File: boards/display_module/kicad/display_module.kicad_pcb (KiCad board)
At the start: 2 copper layers, 58.4 x 148.6 mm, 31 parts, among them IC1 ATMEGA328-P, P1 CONN_01X02, Q1 NDP6020P, Q2 NDP6020P, Q3 NDP6020P, Q4 NDP6020P, Q5 NDP6020P, Q6 NDP6020P, Q7 NDP6020P, Q8 NDP6020P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

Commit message: display module design
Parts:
- moved C1 60.2 mm to (185.4, 44.5)
- moved R8 55.9 mm to (188.0, 52.1)
- moved C4 14.4 mm to (160.0, 52.1)
- moved U2 2.84 mm to (132.1, 64.8)
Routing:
- net Net-(DISP1-Pad9): track 70.5 -> 0.00 mm
- net Net-(DISP1-Pad3): track 70.5 -> 0.00 mm
- net Net-(DISP1-Pad12): track 68.1 -> 0.00 mm
- net Net-(DISP1-Pad6): track 68.1 -> 0.00 mm
- net Net-(DISP1-Pad19): track 59.5 -> 0.00 mm
- net Net-(DISP1-Pad13): track 59.5 -> 0.00 mm
- net Net-(DISP1-Pad16): track 59.5 -> 0.00 mm
- net Net-(DISP1-Pad22): track 59.5 -> 0.00 mm
- net Net-(DISP2-Pad14): track 55.4 -> 0.00 mm
- net Net-(DISP2-Pad1): track 55.4 -> 0.00 mm
- net Net-(DISP2-Pad2): track 54.7 -> 0.00 mm
- net Net-(DISP2-Pad4): track 52.9 -> 0.00 mm
- net Net-(DISP2-Pad5): track 52.2 -> 0.00 mm
- net Net-(DISP2-Pad8): track 47.0 -> 0.00 mm
- net Net-(DISP2-Pad7): track 45.9 -> 0.00 mm
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- removed copper zone on F.Cu, net GND

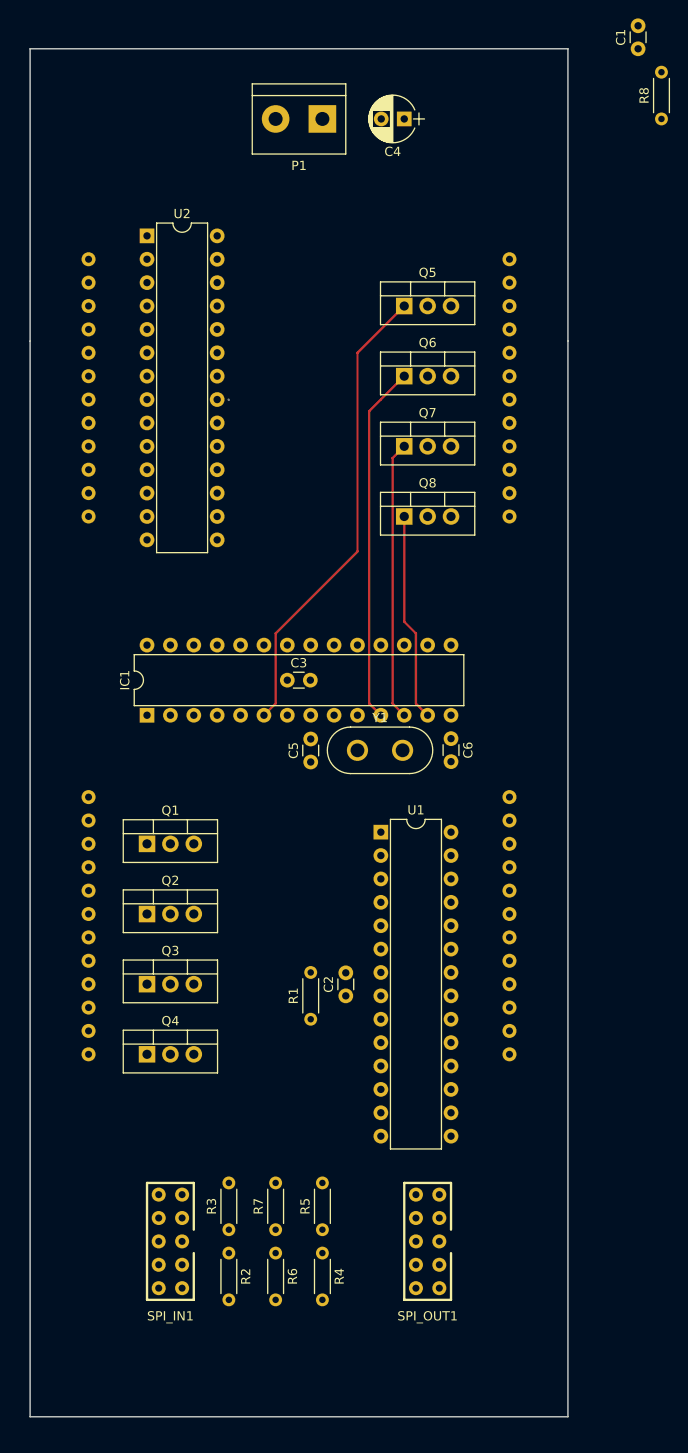
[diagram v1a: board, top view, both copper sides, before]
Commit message: finished display module layout, sent to printing
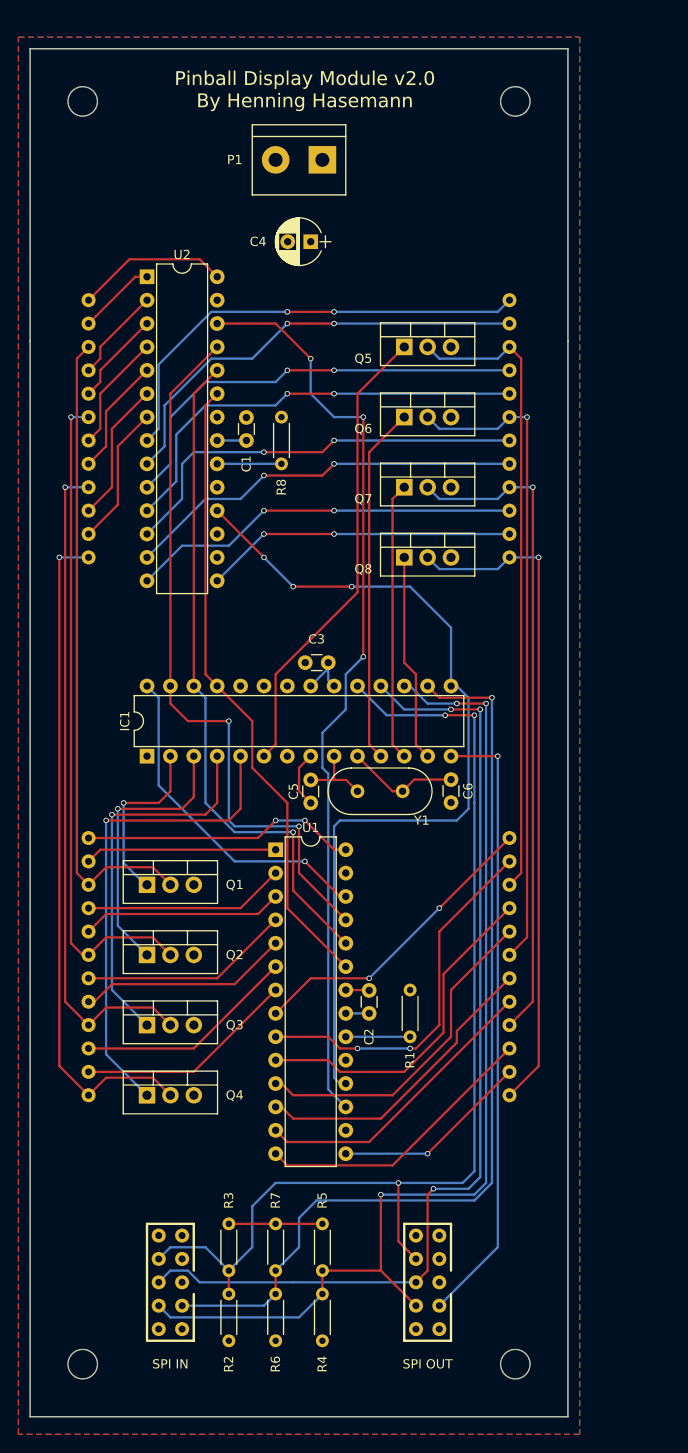
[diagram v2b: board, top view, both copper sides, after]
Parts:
- added ?: , Mounting_Holes:MountingHole_3.2mm_M3_DIN965, F.Cu at (125.1, 50.2)
- added ?: , Mounting_Holes:MountingHole_3.2mm_M3_DIN965, F.Cu at (172.1, 50.2)
- added ?: , Mounting_Holes:MountingHole_3.2mm_M3_DIN965, F.Cu at (172.1, 187.3)
- added ?: , Mounting_Holes:MountingHole_3.2mm_M3_DIN965, F.Cu at (125.1, 187.3)
- SPI IN: renamed from SPI_IN1
- SPI OUT: renamed from SPI_OUT1
- Y1: footprint Crystals:Crystal_HC50_Vertical -> Crystals:Crystal_HC18-U_Vertical
- moved C1 60.2 mm to (142.9, 87.0)
- moved R8 55.7 mm to (146.7, 89.5)
- moved C4 16.8 mm to (149.9, 65.4)
- moved U1 11.6 mm to (146.1, 131.4)
- moved R1 11.0 mm to (160.7, 151.8)
- moved C3 4.84 mm to (151.8, 111.1), turned to 180 degrees
- moved DISP1 4.45 mm to (148.6, 140.3)
- moved Q4 4.45 mm to (132.1, 158.1)
- moved R2 4.45 mm to (141.0, 179.7)
- moved R4 4.45 mm to (151.1, 179.7)
- moved R6 4.45 mm to (146.1, 179.7)
- moved C6 4.45 mm to (165.1, 123.8)
- moved DISP2 4.45 mm to (148.6, 81.9)
- moved Q7 4.45 mm to (160.0, 92.1)
- moved U2 4.45 mm to (132.1, 69.2)
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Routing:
- net Net-(IC1-Pad19): track 0.00 -> 118.1 mm, vias 0 -> 3
- net Net-(IC1-Pad17): track 0.00 -> 115.6 mm, vias 0 -> 3
- net Net-(IC1-Pad18): track 0.00 -> 108.2 mm, vias 0 -> 3
- net Net-(IC1-Pad16): track 0.00 -> 102.7 mm, vias 0 -> 1
- net Net-(U1-Pad17): track 0.00 -> 100.1 mm, vias 0 -> 3
- net Net-(IC1-Pad15): track 0.00 -> 95.7 mm, vias 0 -> 3
- net Net-(IC1-Pad27): track 0.00 -> 78.9 mm, vias 0 -> 2
- net Net-(IC1-Pad26): track 0.00 -> 73.8 mm, vias 0 -> 1
- net Net-(DISP1-Pad13): track 0.00 -> 73.4 mm, vias 0 -> 1
- net Net-(DISP1-Pad12): track 0.00 -> 72.9 mm, vias 0 -> 1
- net Net-(DISP1-Pad16): track 0.00 -> 72.5 mm, vias 0 -> 1
- net Net-(DISP1-Pad9): track 0.00 -> 72.0 mm, vias 0 -> 1
- net Net-(DISP1-Pad19): track 0.00 -> 72.0 mm, vias 0 -> 1
- net Net-(DISP1-Pad6): track 0.00 -> 71.1 mm, vias 0 -> 1
- net Net-(DISP1-Pad22): track 0.00 -> 69.9 mm
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- added copper zone on F.Cu, net GND
- added copper zone on B.Cu, net VCC
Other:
- board text added: "Pinball Display Module v2.0 By Henning Hasemann"

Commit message: WIP: display module PCB design v2.1
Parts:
- removed ? (x4): , Mounting_Holes:MountingHole_3.2mm_M3_DIN965
- removed SPI IN: SW10, my_footprints:SW10
- removed SPI OUT: SW10, my_footprints:SW10
- added J1: SELFTEST, my_footprints:PINS1x2, F.Cu at (144.8, 104.8)
- added J2: AUX, my_footprints:PINS1x2, F.Cu at (141.0, 104.8)
- added R10: 10k, Resistors_ThroughHole:R_Axial_DIN0204_L3.6mm_D1.6mm_P7.62mm_Horizontal, F.Cu at (138.4, 139.7)
- added R11: 10k, Resistors_ThroughHole:R_Axial_DIN0204_L3.6mm_D1.6mm_P7.62mm_Horizontal, F.Cu at (138.4, 147.3)
- added R12: 10k, Resistors_ThroughHole:R_Axial_DIN0204_L3.6mm_D1.6mm_P7.62mm_Horizontal, F.Cu at (138.4, 154.9)
- added R13: 10k, Resistors_ThroughHole:R_Axial_DIN0204_L3.6mm_D1.6mm_P7.62mm_Horizontal, F.Cu at (166.4, 73.0)
- added R14: 10k, Resistors_ThroughHole:R_Axial_DIN0204_L3.6mm_D1.6mm_P7.62mm_Horizontal, F.Cu at (166.4, 80.6)
- added R15: 10k, Resistors_ThroughHole:R_Axial_DIN0204_L3.6mm_D1.6mm_P7.62mm_Horizontal, F.Cu at (166.4, 88.3)
- added R16: 10k, Resistors_ThroughHole:R_Axial_DIN0204_L3.6mm_D1.6mm_P7.62mm_Horizontal, F.Cu at (166.4, 95.9)
- added R9: 10k, Resistors_ThroughHole:R_Axial_DIN0204_L3.6mm_D1.6mm_P7.62mm_Horizontal, F.Cu at (138.4, 132.1)
- added REF**: MountingHole_3.2mm_M3_ISO14580, Mounting_Holes:MountingHole_3.2mm_M3_ISO14580, F.Cu at (171.4, 50.8)
- added REF**: MountingHole_3.2mm_M3_ISO14580, Mounting_Holes:MountingHole_3.2mm_M3_ISO14580, F.Cu at (125.7, 50.8)
- added REF**: MountingHole_3.2mm_M3_ISO14580, Mounting_Holes:MountingHole_3.2mm_M3_ISO14580, F.Cu at (125.7, 186.7)
- added REF**: MountingHole_3.2mm_M3_ISO14580, Mounting_Holes:MountingHole_3.2mm_M3_ISO14580, F.Cu at (171.4, 186.7)
- added SPI_IN1: SW10, my_footprints:SW10, F.Cu at (132.7, 185.4)
- added SPI_OUT1: SW10, my_footprints:SW10, F.Cu at (162.6, 185.4)
- added U3: ICSP, my_footprints:PINS3x2, F.Cu at (125.1, 170.8)
- P1: value CONN_01X02 -> POWER
- R1, R2, R3, R4, R5, R6, R7, R8: footprint Resistors_ThroughHole:R_Axial_DIN0204_L3.6mm_D1.6mm_P5.08mm_Horizontal -> Resistors_ThroughHole:R_Axial_DIN0204_L3.6mm_D1.6mm_P7.62mm_Horizontal
- Y1: footprint Crystals:Crystal_HC18-U_Vertical -> Crystals:Crystal_HC50_Vertical
- moved Q1 1.27 mm to (132.1, 136.5)
- moved Q2 1.27 mm to (132.1, 144.1)
- moved DISP1 1.27 mm to (148.6, 141.6)
- moved Q3 1.27 mm to (132.1, 151.8)
- moved Q4 1.27 mm to (132.1, 159.4)
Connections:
- IC1 pad 1: (no net) -> Net-(IC1-Pad1)
- IC1 pad 23: (no net) -> Net-(IC1-Pad23)
- IC1 pad 24: (no net) -> Net-(IC1-Pad24)
- U1 pad 16: (no net) -> Net-(U1-Pad16)
- U2 pad 16: (no net) -> Net-(U2-Pad16)
- U2 pad 17: (no net) -> Net-(U2-Pad17)
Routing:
- net Net-(IC1-Pad1): track 0.00 -> 58.0 mm
- net VCC: track 22.0 -> 51.5 mm
- net GND: track 8.69 -> 25.4 mm, vias 0 -> 2
- net Net-(IC1-Pad17): track 115.6 -> 131.3 mm, vias 3 -> 5
- net Net-(IC1-Pad19): track 118.1 -> 133.6 mm, vias 3 -> 4
- net Net-(IC1-Pad14): track 67.4 -> 60.6 mm, vias 1 -> 4
- net Net-(IC1-Pad16): track 102.7 -> 96.8 mm, vias 1 -> 8
- net Net-(IC1-Pad12): track 30.3 -> 36.2 mm
- net Net-(IC1-Pad5): track 52.5 -> 46.7 mm
- net Net-(IC1-Pad11): track 38.9 -> 43.3 mm, vias 0 -> 1
- net Net-(IC1-Pad24): track 0.00 -> 4.34 mm
- net Net-(IC1-Pad13): track 22.6 -> 27.0 mm
- net Net-(IC1-Pad6): track 50.8 -> 55.1 mm, vias 0 -> 2
- net Net-(DISP1-Pad1): track 33.3 -> 37.6 mm, vias 2 -> 0
- net Net-(IC1-Pad23): track 0.00 -> 3.81 mm
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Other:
- board text added: "Pinball Display Module v2.1 By Henning Hasemann"
- board text removed: "Pinball Display Module v2.0 By Henning Hasemann"

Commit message: WIP: display module PCB design v2.1
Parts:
- ? (x2): renamed from REF**; value MountingHole_3.2mm_M3_ISO14580 -> (none)
- TEST: renamed from J1; value SELFTEST -> TEST
- moved AUX 1.27 mm to (142.2, 104.8)
- renumbered REF** to ?, J2 to AUX, U3 to ICSP, SPI_IN1 to IN, SPI_OUT1 to OUT, P1 to PWR
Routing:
- net Net-(DISP1-Pad1): track 37.6 -> 41.0 mm
- net Net-(IC1-Pad17): track 131.3 -> 129.1 mm, vias 5 -> 3
- net Net-(DISP1-Pad6): track 72.3 -> 70.3 mm, vias 1 -> 2
- net Net-(DISP1-Pad9): track 73.2 -> 72.0 mm
- net Net-(IC1-Pad15): track 95.7 -> 94.8 mm
- net Net-(IC1-Pad18): track 106.3 -> 107.1 mm, vias 7 -> 5
- net Net-(IC1-Pad24): track 4.34 -> 3.81 mm
- net Net-(DISP1-Pad3): track 70.7 -> 71.2 mm, vias 0 -> 1
- net Net-(IC1-Pad19): track 133.6 -> 134.0 mm, vias 4 -> 2
- net Net-(IC1-Pad16): vias 8 -> 6
- net Net-(IC1-Pad14): vias 4 -> 2
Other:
- board text added: "5V"
- board text added: "GND"
- board text added: "Pinball Display Module v2.1 Henning Hasemann 04/2017"
- board text removed: "Pinball Display Module v2.1 By Henning Hasemann"

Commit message: Display Module PCB v2.1
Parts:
- ? (x2): value MountingHole_3.2mm_M3_ISO14580 -> (none)
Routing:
- net Net-(DISP1-Pad13): track 74.6 -> 81.5 mm
- net Net-(DISP1-Pad19): track 72.9 -> 79.0 mm, vias 1 -> 0
- net Net-(DISP1-Pad16): track 73.8 -> 79.0 mm, vias 1 -> 0
- net VCC: track 51.5 -> 55.2 mm
- net Net-(DISP1-Pad22): track 71.2 -> 69.3 mm, vias 0 -> 1
- net Net-(DISP1-Pad9): track 72.0 -> 71.2 mm, vias 1 -> 0
